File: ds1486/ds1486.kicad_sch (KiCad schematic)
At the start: 74 parts, among them J1 DBG, J2 DBG1-16, J3 DBG17-32, J4 DS1-16, J5 DS17-32, U1 RP2040, U3 AMS1117-3.3, U4 SN74LVC8T245, U5 SN74LVC1G00DRL, U6 YSN8010SJ, U7 SN74LVC1G00DRL, U8 W25Q16JVSS, Y2 E3SB12E00004EE

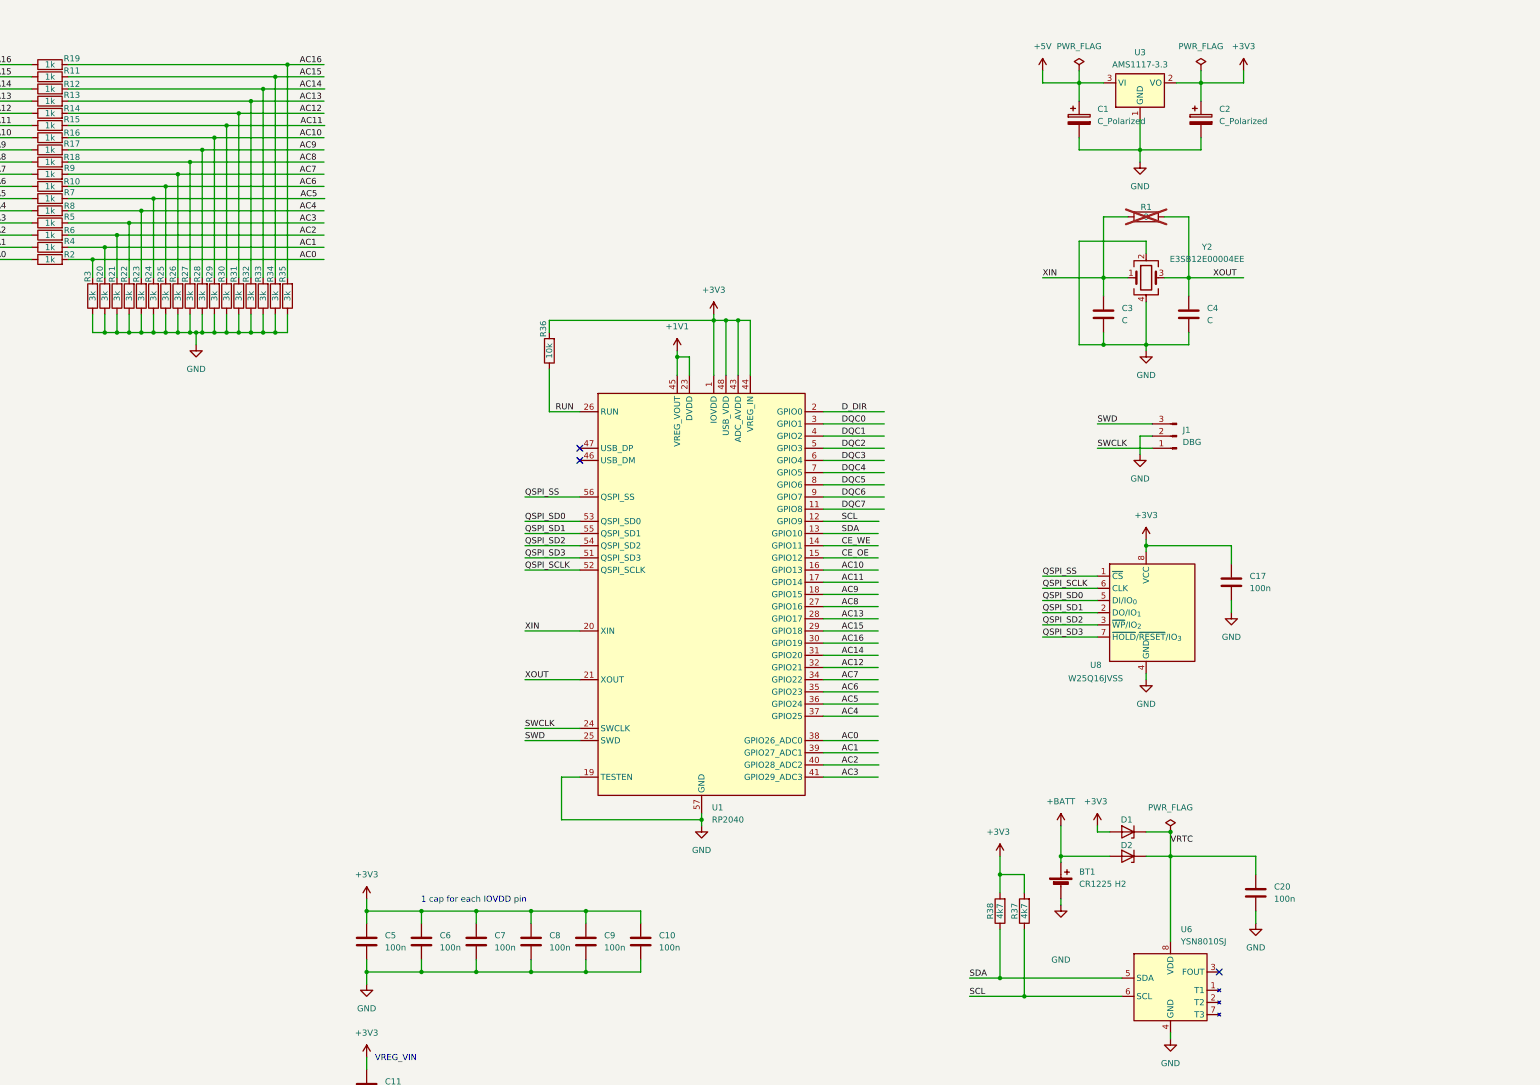
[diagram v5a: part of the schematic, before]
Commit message: Move VRTC and SPI flash to front layer.
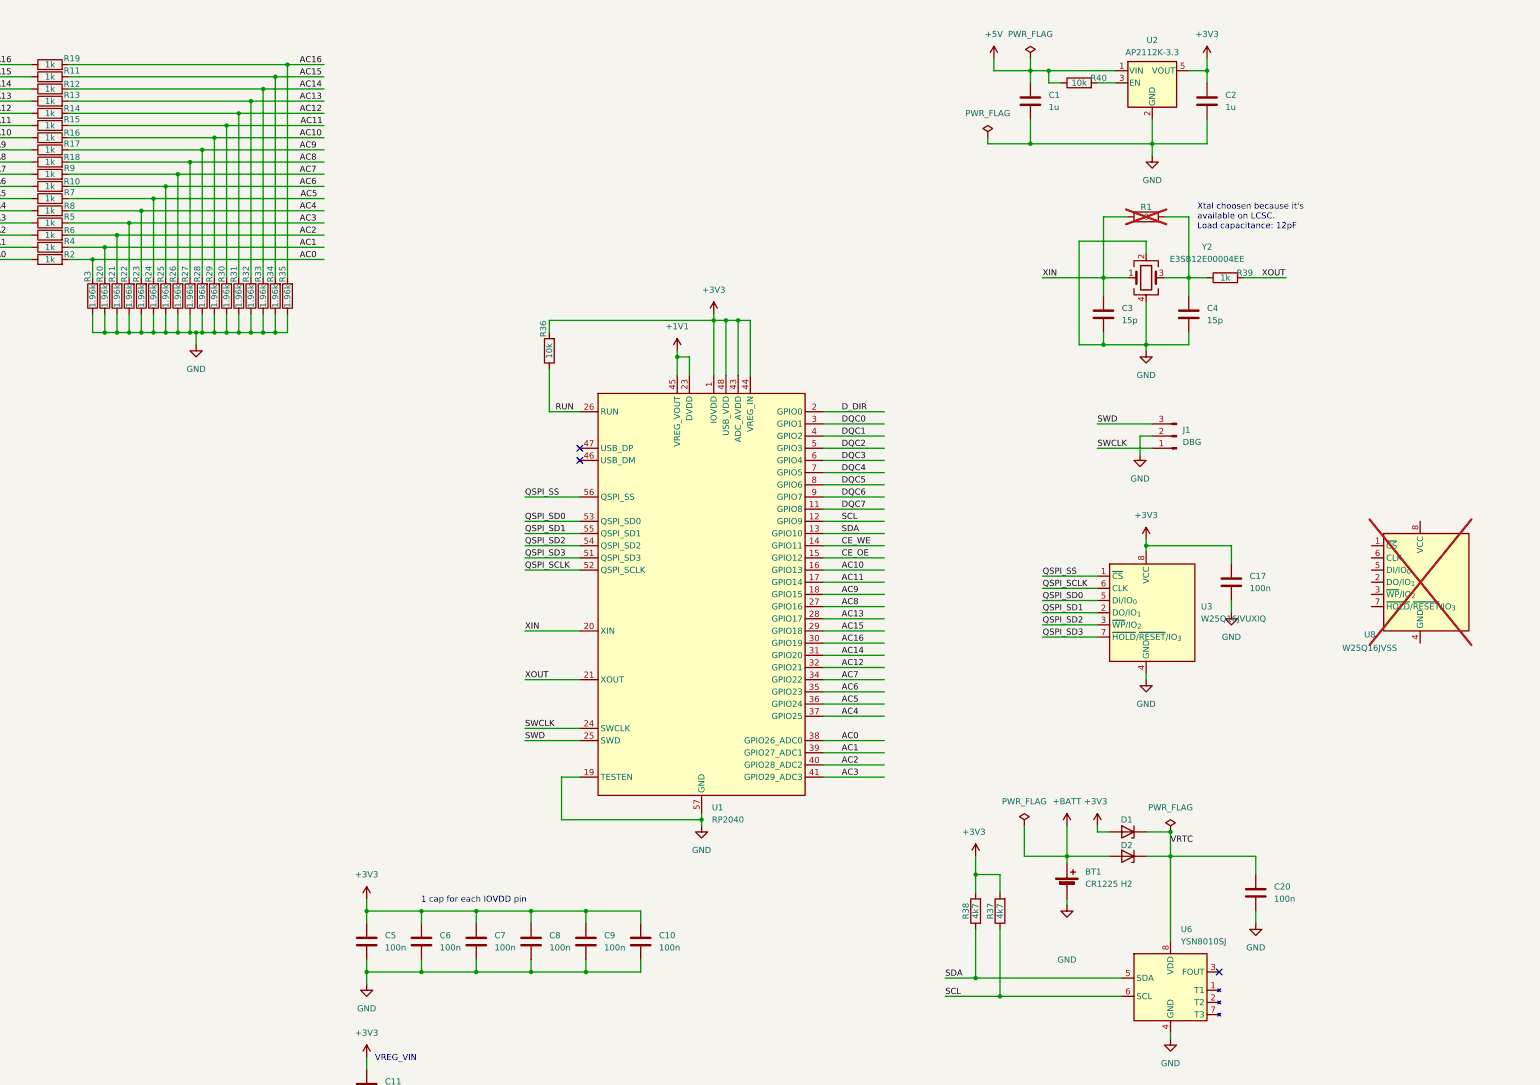
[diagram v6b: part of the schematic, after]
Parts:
- removed C1, C2: C_Polarized, Capacitor_SMD:C_0805_2012Metric, symbol Device:C_Polarized
- removed U3: AMS1117-3.3, Package_TO_SOT_SMD:SOT-223-3_TabPin2, symbol Regulator_Linear:AMS1117-3.3
- added C1, C2: 1u, Capacitor_SMD:C_0603_1608Metric, symbol Device:C
- added R39: 1k, Resistor_SMD:R_0402_1005Metric, symbol Device:R
- added R40: 10k, Resistor_SMD:R_0402_1005Metric, symbol Device:R
- added U2: AP2112K-3.3, Package_TO_SOT_SMD:SOT-23-5, symbol Regulator_Linear:AP2112K-3.3
- added U3: W25Q16JVUXIQ, Package_SON:Winbond_USON-8-1EP_3x2mm_P0.5mm_EP0.2x1.6mm, symbol Kicad_Personal:W25Q16JVUXIQ
- C3, C4: value C -> 15p
- R20, R21, R22, R23, R24, R25, R26, R27, R28, R29, R3, R30, R31, R32, R33, R34, R35: value 3k -> 1.96k
- U8: now not fitted; now left out of the parts list
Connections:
- net +3V3: now also C2.1, U2.5 (VOUT), U3.8 (VCC); no longer U8.8 (VCC)
- net +5V: now also C1.1, R40.1, U2.1 (VIN)
- net GND: now also C1.2, C2.2, U2.2 (GND), U3.4 (GND); no longer U8.4 (GND)
- net QSPI_SCLK: now also U3.6 (CLK); no longer U8.6 (CLK)
- net QSPI_SD0: now also U3.5 (DI/IO_{0}); no longer U8.5 (DI/IO_{0})
- net QSPI_SD1: now also U3.2 (DO/IO_{1}); no longer U8.2 (DO/IO_{1})
- net QSPI_SD2: now also U3.3 (~{WP}/IO_{2}); no longer U8.3 (~{WP}/IO_{2})
- net QSPI_SD3: now also U3.7 (~{HOLD}/~{RESET}/IO_{3}); no longer U8.7 (~{HOLD}/~{RESET}/IO_{3})
- net QSPI_SS: now also U3.1 (~{CS}); no longer U8.1 (~{CS})
- net XOUT: now also R39.2; no longer C4.1, R1.2, Y2.3
- new net: C4.1, R1.2, R39.1, Y2.3
- new net: R40.2, U2.3 (EN)
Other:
- note added: "Xtal choosen because it's available on LCSC. Load capacitance: 12pF"
- moved on the sheet: BT1, R37, R38

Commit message: Move D_DIR.
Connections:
- net DQC0: now also U1.2 (GPIO0); no longer U1.3 (GPIO1)
- net DQC1: now also U1.3 (GPIO1); no longer U1.4 (GPIO2)
- net DQC2: now also U1.4 (GPIO2); no longer U1.5 (GPIO3)
- net DQC3: now also U1.5 (GPIO3); no longer U1.6 (GPIO4)
- net DQC4: now also U1.6 (GPIO4); no longer U1.7 (GPIO5)
- net DQC5: now also U1.7 (GPIO5); no longer U1.8 (GPIO6)
- net DQC6: now also U1.8 (GPIO6); no longer U1.9 (GPIO7)
- net DQC7: now also U1.9 (GPIO7); no longer U1.11 (GPIO8)
- net D_DIR: now also U1.11 (GPIO8); no longer U1.2 (GPIO0)
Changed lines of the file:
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@@
 	(wire
 		(pts
-			(xy 304.8 97.79) (xy 317.5 97.79)
+			(xy 304.8 118.11) (xy 317.5 118.11)
 		)
 		(stroke
@@
 	(wire
 		(pts
-			(xy 304.8 113.03) (xy 317.5 113.03)
+			(xy 304.8 110.49) (xy 317.5 110.49)
 		)
 		(stroke
@@
 	(wire
 		(pts
-			(xy 304.8 118.11) (xy 317.5 118.11)
+			(xy 304.8 115.57) (xy 317.5 115.57)
 		)
 		(stroke
@@
 	(wire
 		(pts
-			(xy 304.8 102.87) (xy 317.5 102.87)
+			(xy 304.8 100.33) (xy 317.5 100.33)
 		)
 		(stroke
@@
 	(wire
 		(pts
-			(xy 304.8 105.41) (xy 317.5 105.41)
+			(xy 304.8 102.87) (xy 317.5 102.87)
 		)
 		(stroke
@@
 	(wire
 		(pts
-			(xy 304.8 115.57) (xy 317.5 115.57)
+			(xy 304.8 113.03) (xy 317.5 113.03)
 		)
 		(stroke
@@
 	(wire
 		(pts
-			(xy 304.8 107.95) (xy 317.5 107.95)
+			(xy 304.8 105.41) (xy 317.5 105.41)
 		)
 		(stroke
@@
 	(wire
 		(pts
-			(xy 304.8 110.49) (xy 317.5 110.49)
+			(xy 304.8 107.95) (xy 317.5 107.95)
 		)
 		(stroke
@@
 	(wire
 		(pts
-			(xy 304.8 100.33) (xy 317.5 100.33)
+			(xy 304.8 97.79) (xy 317.5 97.79)
 		)
 		(stroke
@@
 	)
 	(label "DQC3"
-		(at 308.61 107.95 0)
+		(at 308.61 105.41 0)
 		(effects
 			(font
@@
 	)
 	(label "DQC1"
-		(at 308.61 102.87 0)
+		(at 308.61 100.33 0)
 		(effects
 			(font
@@
 	)
 	(label "DQC0"
-		(at 308.61 100.33 0)
+		(at 308.61 97.79 0)
 		(effects
 			(font
@@
 	)
 	(label "DQC5"
-		(at 308.61 113.03 0)
+		(at 308.61 110.49 0)
 		(effects
 			(font
@@
 	)
 	(label "DQC4"
-		(at 308.61 110.49 0)
+		(at 308.61 107.95 0)
 		(effects
 			(font
@@
 	)
 	(label "DQC2"
-		(at 308.61 105.41 0)
+		(at 308.61 102.87 0)
 		(effects
 			(font
@@
 	)
 	(label "DQC6"
-		(at 308.61 115.57 0)
+		(at 308.61 113.03 0)
 		(effects
 			(font
@@
 	)
 	(label "DQC7"
-		(at 308.61 118.11 0)
+		(at 308.61 115.57 0)
 		(effects
 			(font
@@
 	)
 	(label "D_DIR"
-		(at 308.61 97.79 0)
+		(at 308.61 118.11 0)
 		(effects
 			(font

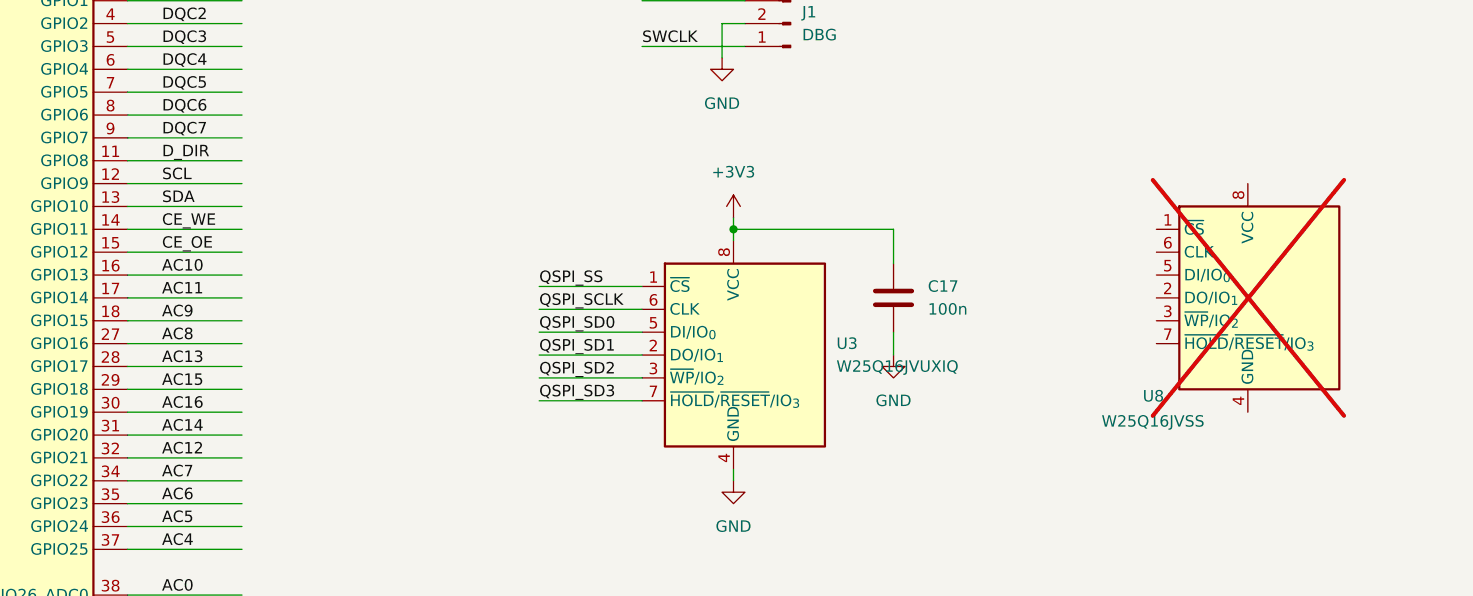
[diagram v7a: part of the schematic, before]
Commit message: Remove old W25Q16.
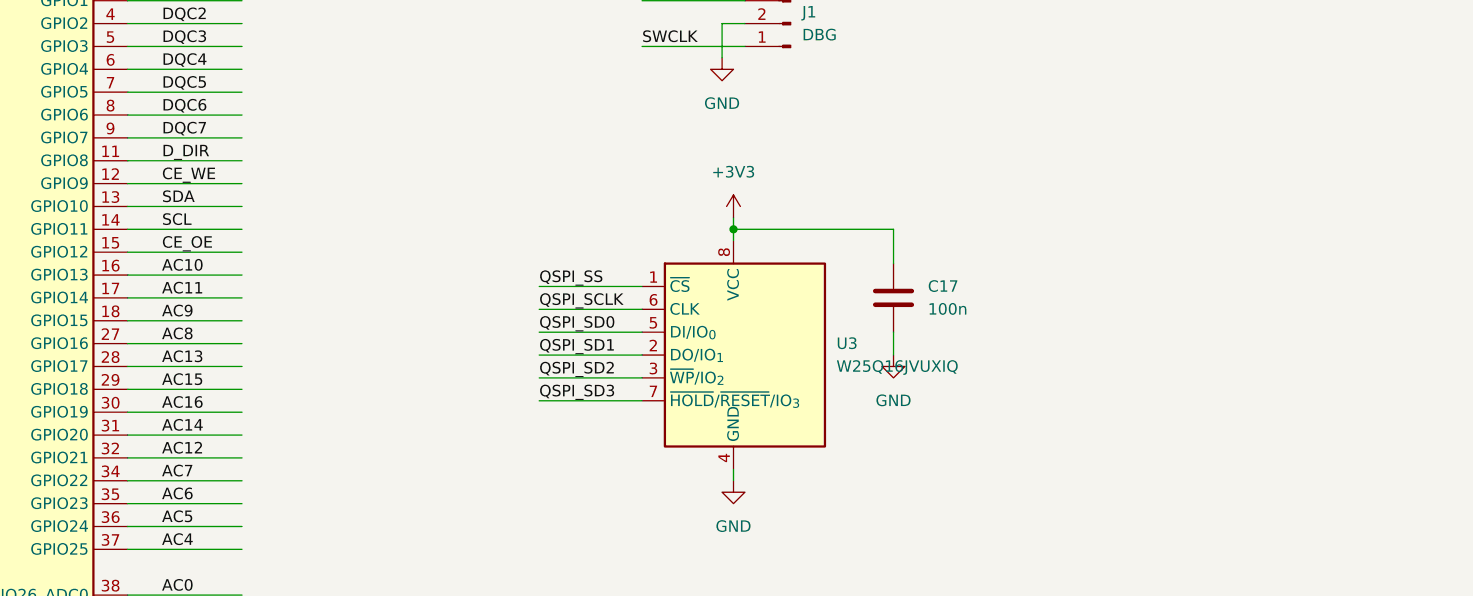
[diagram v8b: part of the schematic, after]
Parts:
- removed U8: W25Q16JVSS, Package_SO:SOIC-8_5.3x5.3mm_P1.27mm, symbol Memory_Flash:W25Q16JVSS
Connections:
- net CE_WE: now also U1.12 (GPIO9); no longer U1.14 (GPIO11)
- net SCL: now also U1.14 (GPIO11); no longer U1.12 (GPIO9)
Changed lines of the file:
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@@
 	)
 	(label "SCL"
-		(at 308.61 120.65 0)
+		(at 308.61 125.73 0)
 		(effects
 			(font
@@
 	)
 	(label "CE_WE"
-		(at 308.61 125.73 0)
+		(at 308.61 120.65 0)
 		(effects
 			(font
@@
 					(unit 1)
 				)
-			)
-		)
-	)
-	(symbol
-		(lib_id "Memory_Flash:W25Q16JVSS")
-		(at 429.26 133.35 0)
-		(unit 1)
-		(exclude_from_sim yes)
-		(in_bom no)
-		(on_board no)
-		(dnp yes)
-		(property "Reference" "U8"
-			(at 417.576 144.272 0)
-			(effects
-				(font
-					(size 1.27 1.27)
-				)
-				(justify left)
-			)
-		)
-		(property "Value" "W25Q16JVSS"
-			(at 413.004 147.066 0)
-			(effects
-				(font
-					(size 1.27 1.27)
-				)
-				(justify left)
-			)
-		)
-		(property "Footprint" "Package_SO:SOIC-8_5.3x5.3mm_P1.27mm"
-			(at 429.26 133.35 0)
-			(effects
-				(font
-					(size 1.27 1.27)
-				)
-				(hide yes)
-			)
-		)
-		(property "Datasheet" "https://www.winbond.com/hq/support/documentation/levelOne.jsp?__locale=en&DocNo=DA00-W25Q16JV.1"
-			(at 429.26 133.35 0)
-			(effects
-				(font
-					(size 1.27 1.27)
-				)
-				(hide yes)
-			)
-		)
-		(property "Description" "16Mbit / 2MiB Serial Flash Memory, Standard/Dual/Quad SPI, 2.7-3.6V, SOIC-8 (208 mil)"
-			(at 429.26 133.35 0)
-			(effects
-				(font
-					(size 1.27 1.27)
-				)
-				(hide yes)
-			)
-		)
-		(pin "4"
-		)
-		(pin "7"
-		)
-		(pin "5"
-		)
-		(pin "8"
-		)
-		(pin "3"
-		)
-		(pin "6"
-		)
-		(pin "2"
-		)
-		(pin "1"
-		)
-		(instances
-			(project ""
-				(path "/60dea446-8117-48c7-bbf2-f1b5c8a0ff90"
-					(reference "U8")
-					(unit 1)
-				)
